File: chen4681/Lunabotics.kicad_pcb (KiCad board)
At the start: 2 copper layers, 55.7 x 31.3 mm, 11 parts, among them J1 Conn_01x02_Socket, J2 Conn_01x02_Socket, U1 ACS711xLCTR-12AB, U2 mcp6546-e/p

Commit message: Changed decoup-cap locations and track widths
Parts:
- moved C1 2.48 mm to (94.0, 68.5)
- moved C2 1.52 mm to (96.5, 68.5)
- moved D1 1.25 mm to (118.7, 81.3)
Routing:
- net +3V3: track 106.7 -> 108.2 mm
- net Net-(D1-A): track 6.66 -> 7.88 mm
- net Net-(U1-VIOUT): track 44.2 -> 43.2 mm
- net GND: track 53.0 -> 52.5 mm

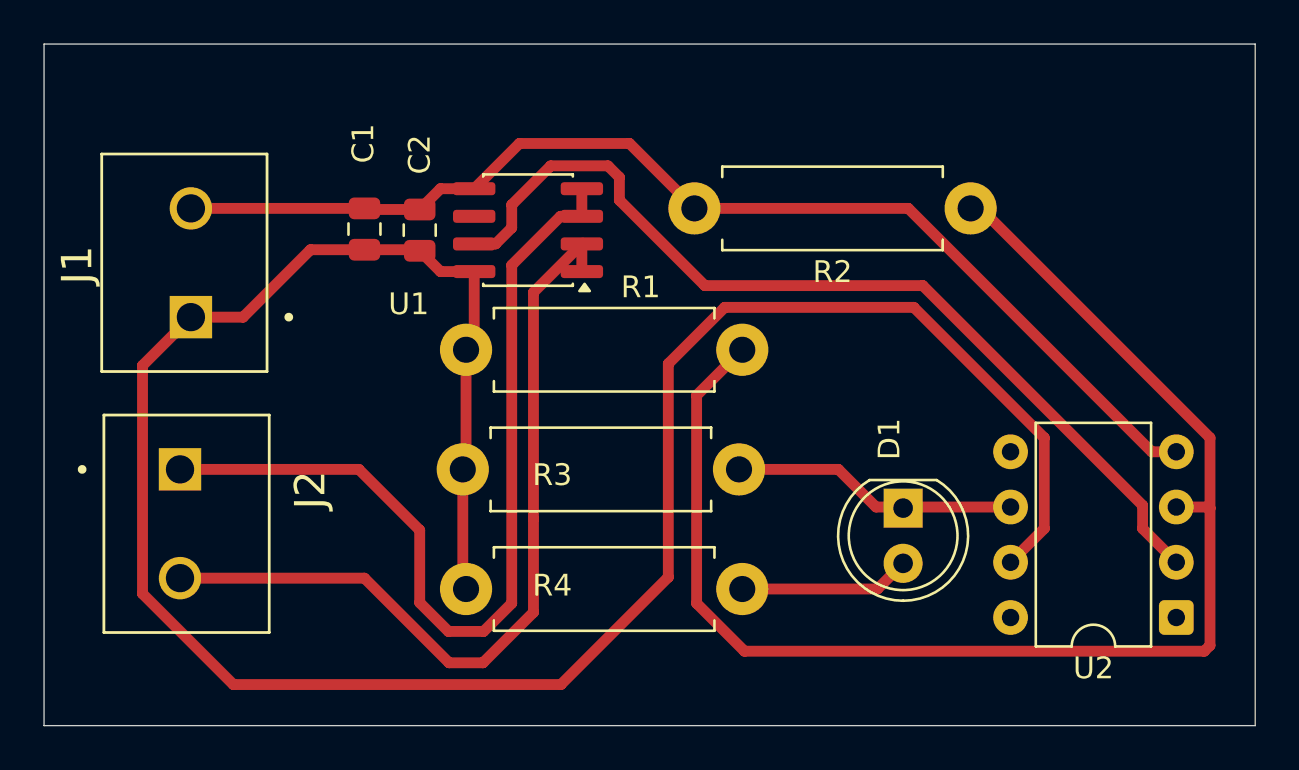
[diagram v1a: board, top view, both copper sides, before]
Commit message: Reworked C1 to be next to U2
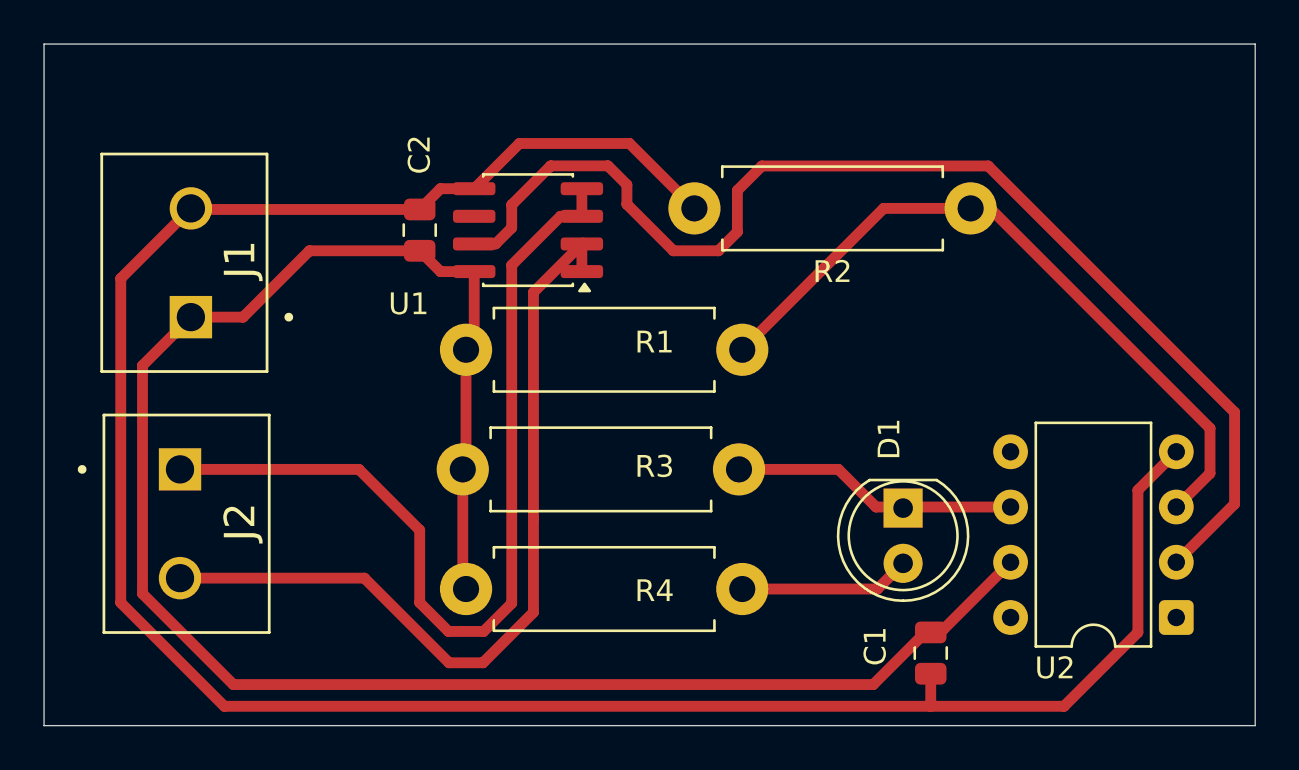
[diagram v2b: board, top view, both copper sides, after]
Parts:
- moved C1 32.5 mm to (120.0, 87.9), turned to 90 degrees
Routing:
- net GND: track 52.5 -> 105.9 mm
- net Net-(U2-VIN+): track 63.6 -> 32.6 mm
- net +3V3: track 108.2 -> 87.2 mm
- net Net-(U1-VIOUT): track 43.2 -> 54.6 mm
